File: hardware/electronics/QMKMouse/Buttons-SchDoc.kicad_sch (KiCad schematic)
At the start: 8 parts

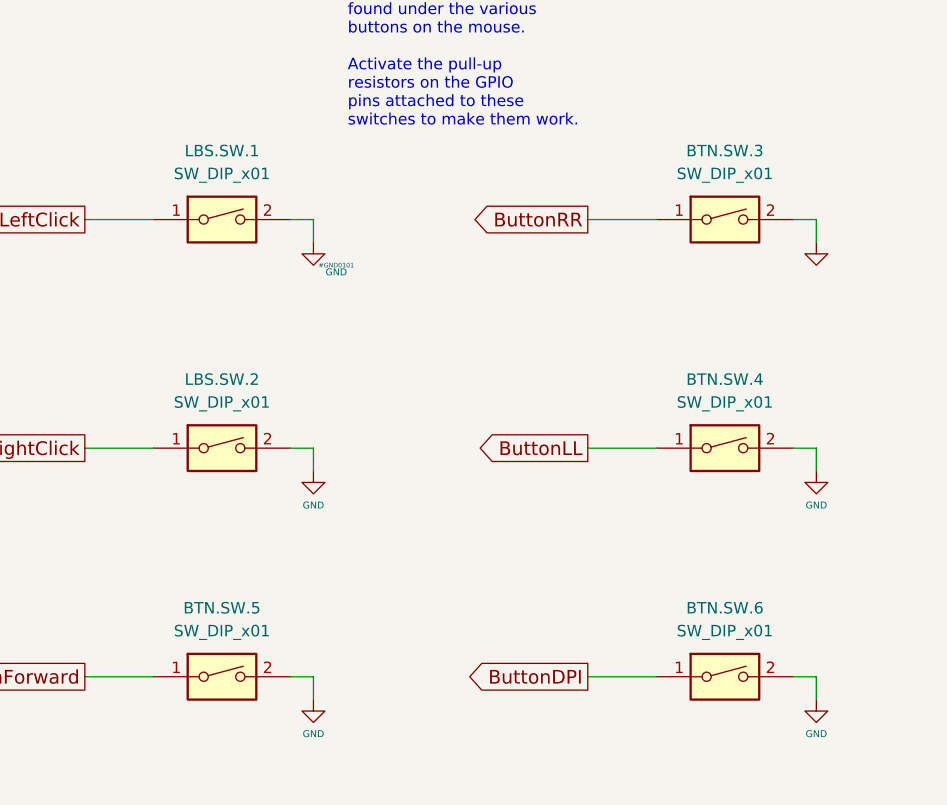
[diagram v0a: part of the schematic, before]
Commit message: update schematic components
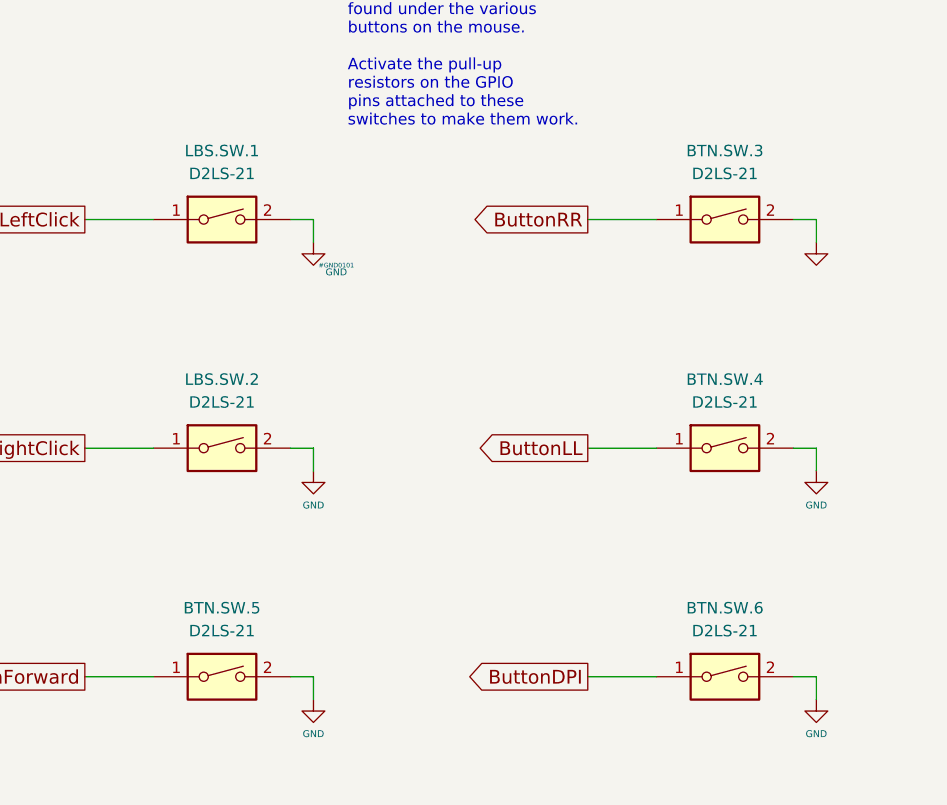
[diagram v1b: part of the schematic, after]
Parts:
- BTN.SW.3, BTN.SW.4, BTN.SW.5, BTN.SW.6, LBS.SW.1, LBS.SW.2: value SW_DIP_x01 -> D2LS-21
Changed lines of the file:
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@@
     (in_bom yes) (on_board yes) (fields_autoplaced)
     (property "Reference" "LBS.SW.2" (id 0) (at 91.44 87.63 0))
-    (property "Value" "SW_DIP_x01" (id 1) (at 91.44 90.17 0))
+    (property "Value" "D2LS-21" (id 1) (at 91.44 90.17 0))
     (property "Footprint" "" (id 2) (at 91.44 95.25 0)
       (effects (font (size 1.27 1.27)) hide)
@@
     (in_bom yes) (on_board yes) (fields_autoplaced)
     (property "Reference" "BTN.SW.4" (id 0) (at 147.32 87.63 0))
-    (property "Value" "SW_DIP_x01" (id 1) (at 147.32 90.17 0))
+    (property "Value" "D2LS-21" (id 1) (at 147.32 90.17 0))
     (property "Footprint" "" (id 2) (at 147.32 95.25 0)
       (effects (font (size 1.27 1.27)) hide)
@@
     (in_bom yes) (on_board yes) (fields_autoplaced)
     (property "Reference" "BTN.SW.6" (id 0) (at 147.32 113.03 0))
-    (property "Value" "SW_DIP_x01" (id 1) (at 147.32 115.57 0))
+    (property "Value" "D2LS-21" (id 1) (at 147.32 115.57 0))
     (property "Footprint" "" (id 2) (at 147.32 120.65 0)
       (effects (font (size 1.27 1.27)) hide)
@@
     (in_bom yes) (on_board yes) (fields_autoplaced)
     (property "Reference" "BTN.SW.5" (id 0) (at 91.44 113.03 0))
-    (property "Value" "SW_DIP_x01" (id 1) (at 91.44 115.57 0))
+    (property "Value" "D2LS-21" (id 1) (at 91.44 115.57 0))
     (property "Footprint" "" (id 2) (at 91.44 120.65 0)
       (effects (font (size 1.27 1.27)) hide)
@@
     (in_bom yes) (on_board yes) (fields_autoplaced)
     (property "Reference" "LBS.SW.1" (id 0) (at 91.44 62.23 0))
-    (property "Value" "SW_DIP_x01" (id 1) (at 91.44 64.77 0))
+    (property "Value" "D2LS-21" (id 1) (at 91.44 64.77 0))
     (property "Footprint" "" (id 2) (at 91.44 69.85 0)
       (effects (font (size 1.27 1.27)) hide)
@@
     (in_bom yes) (on_board yes) (fields_autoplaced)
     (property "Reference" "BTN.SW.3" (id 0) (at 147.32 62.23 0))
-    (property "Value" "SW_DIP_x01" (id 1) (at 147.32 64.77 0))
+    (property "Value" "D2LS-21" (id 1) (at 147.32 64.77 0))
     (property "Footprint" "" (id 2) (at 147.32 69.85 0)
       (effects (font (size 1.27 1.27)) hide)

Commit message: update schematic from PCB; sync netlist and fix some symbol orientations; also fix LED symbol
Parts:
- BTN.SW.3, BTN.SW.4, BTN.SW.5, BTN.SW.6, BTN.SW.7, BTN.SW.8, LBS.SW.1, LBS.SW.2: footprint (none) -> Switches.PcbLib:D2LS-21
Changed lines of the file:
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@@
     (property "Reference" "BTN.SW.7" (id 0) (at 91.44 138.43 0))
     (property "Value" "SW_DIP_x01" (id 1) (at 91.44 140.97 0))
-    (property "Footprint" "" (id 2) (at 91.44 146.05 0)
+    (property "Footprint" "Switches.PcbLib:D2LS-21" (id 2) (at 91.44 146.05 0)
       (effects (font (size 1.27 1.27)) hide)
     )
@@
     (property "Reference" "LBS.SW.2" (id 0) (at 91.44 87.63 0))
     (property "Value" "D2LS-21" (id 1) (at 91.44 90.17 0))
-    (property "Footprint" "" (id 2) (at 91.44 95.25 0)
+    (property "Footprint" "Switches.PcbLib:D2LS-21" (id 2) (at 91.44 95.25 0)
       (effects (font (size 1.27 1.27)) hide)
     )
@@
     (property "Reference" "BTN.SW.4" (id 0) (at 147.32 87.63 0))
     (property "Value" "D2LS-21" (id 1) (at 147.32 90.17 0))
-    (property "Footprint" "" (id 2) (at 147.32 95.25 0)
+    (property "Footprint" "Switches.PcbLib:D2LS-21" (id 2) (at 147.32 95.25 0)
       (effects (font (size 1.27 1.27)) hide)
     )
@@
     (property "Reference" "BTN.SW.6" (id 0) (at 147.32 113.03 0))
     (property "Value" "D2LS-21" (id 1) (at 147.32 115.57 0))
-    (property "Footprint" "" (id 2) (at 147.32 120.65 0)
+    (property "Footprint" "Switches.PcbLib:D2LS-21" (id 2) (at 147.32 120.65 0)
       (effects (font (size 1.27 1.27)) hide)
     )
@@
     (property "Reference" "BTN.SW.8" (id 0) (at 147.32 138.43 0))
     (property "Value" "SW_DIP_x01" (id 1) (at 147.32 140.97 0))
-    (property "Footprint" "" (id 2) (at 147.32 146.05 0)
+    (property "Footprint" "Switches.PcbLib:D2LS-21" (id 2) (at 147.32 146.05 0)
       (effects (font (size 1.27 1.27)) hide)
     )
@@
     (property "Reference" "BTN.SW.5" (id 0) (at 91.44 113.03 0))
     (property "Value" "D2LS-21" (id 1) (at 91.44 115.57 0))
-    (property "Footprint" "" (id 2) (at 91.44 120.65 0)
+    (property "Footprint" "Switches.PcbLib:D2LS-21" (id 2) (at 91.44 120.65 0)
       (effects (font (size 1.27 1.27)) hide)
     )
@@
     (property "Reference" "LBS.SW.1" (id 0) (at 91.44 62.23 0))
     (property "Value" "D2LS-21" (id 1) (at 91.44 64.77 0))
-    (property "Footprint" "" (id 2) (at 91.44 69.85 0)
+    (property "Footprint" "Switches.PcbLib:D2LS-21" (id 2) (at 91.44 69.85 0)
       (effects (font (size 1.27 1.27)) hide)
     )
@@
     (property "Reference" "BTN.SW.3" (id 0) (at 147.32 62.23 0))
     (property "Value" "D2LS-21" (id 1) (at 147.32 64.77 0))
-    (property "Footprint" "" (id 2) (at 147.32 69.85 0)
+    (property "Footprint" "Switches.PcbLib:D2LS-21" (id 2) (at 147.32 69.85 0)
       (effects (font (size 1.27 1.27)) hide)
     )

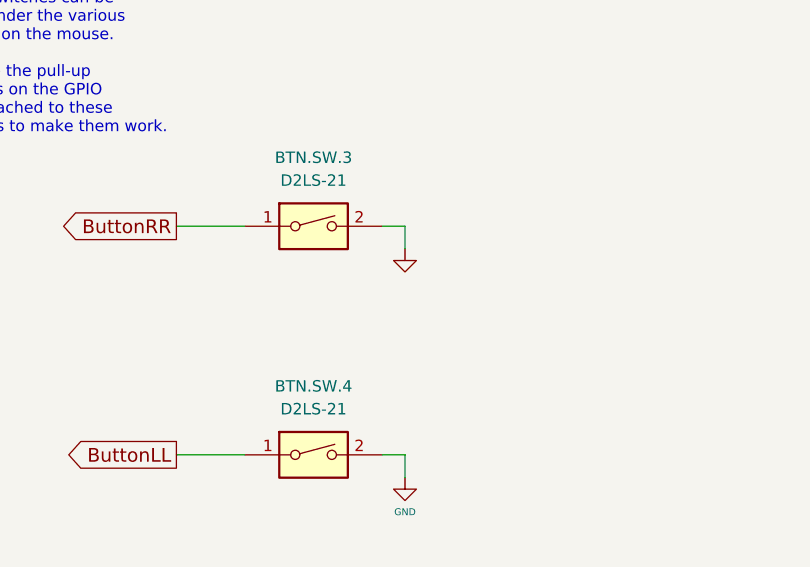
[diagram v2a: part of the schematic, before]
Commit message: Fix some schematic PCB mismatch
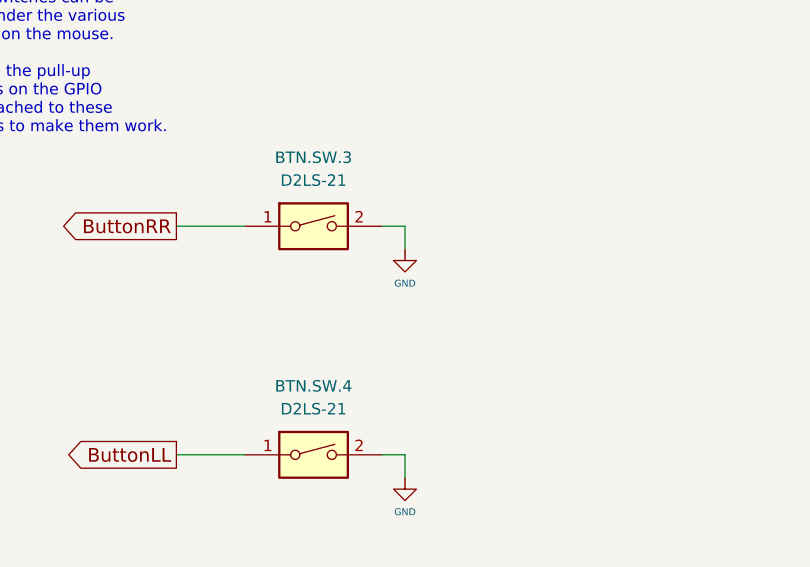
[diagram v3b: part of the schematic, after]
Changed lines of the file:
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@@
       (effects (font (size 0.508 0.508)) hide)
     )
-    (property "Value" "GND" (id 1) (at 160.02 75.692 0)
-      (effects (font (size 0.762 0.762)) hide)
+    (property "Value" "GND" (id 1) (at 157.48 76.2 0)
+      (effects (font (size 0.762 0.762)))
     )
     (property "Footprint" "" (id 2) (at 157.48 72.39 0)

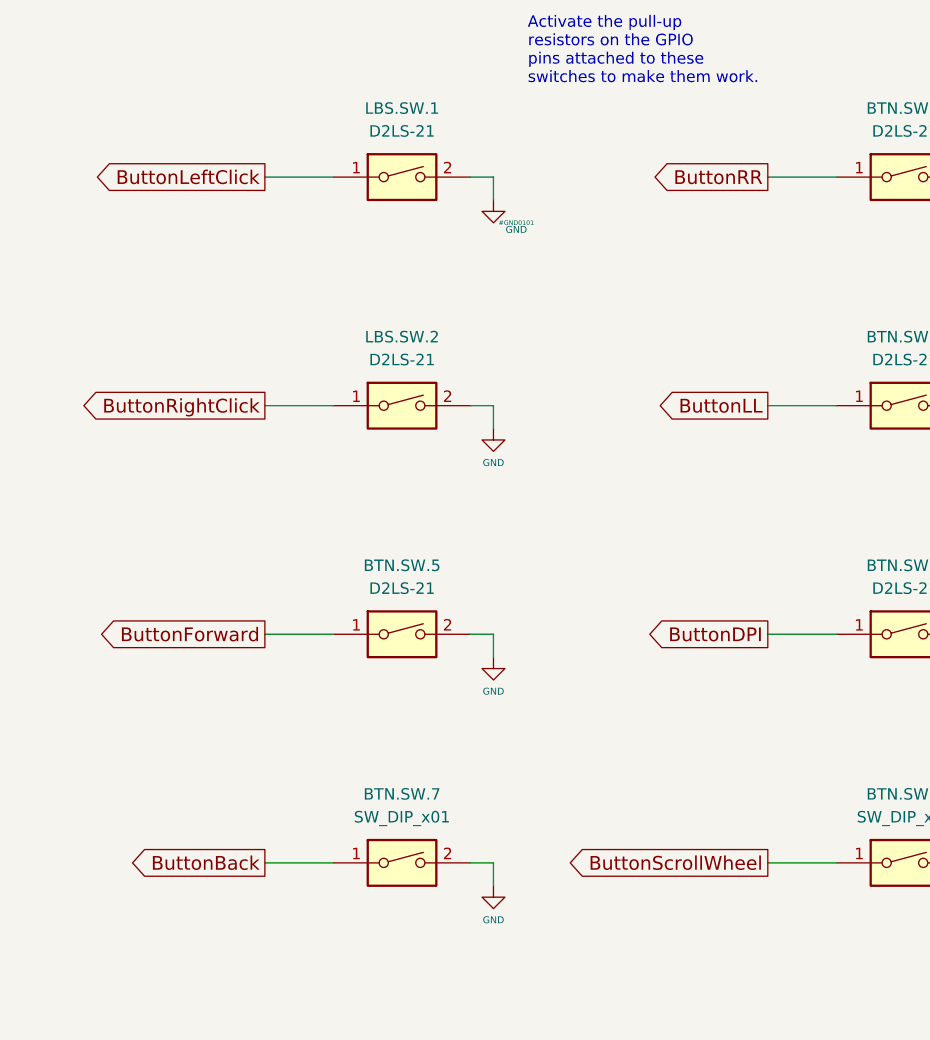
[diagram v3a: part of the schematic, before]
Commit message: fix ERC errors and use hierarchy labels
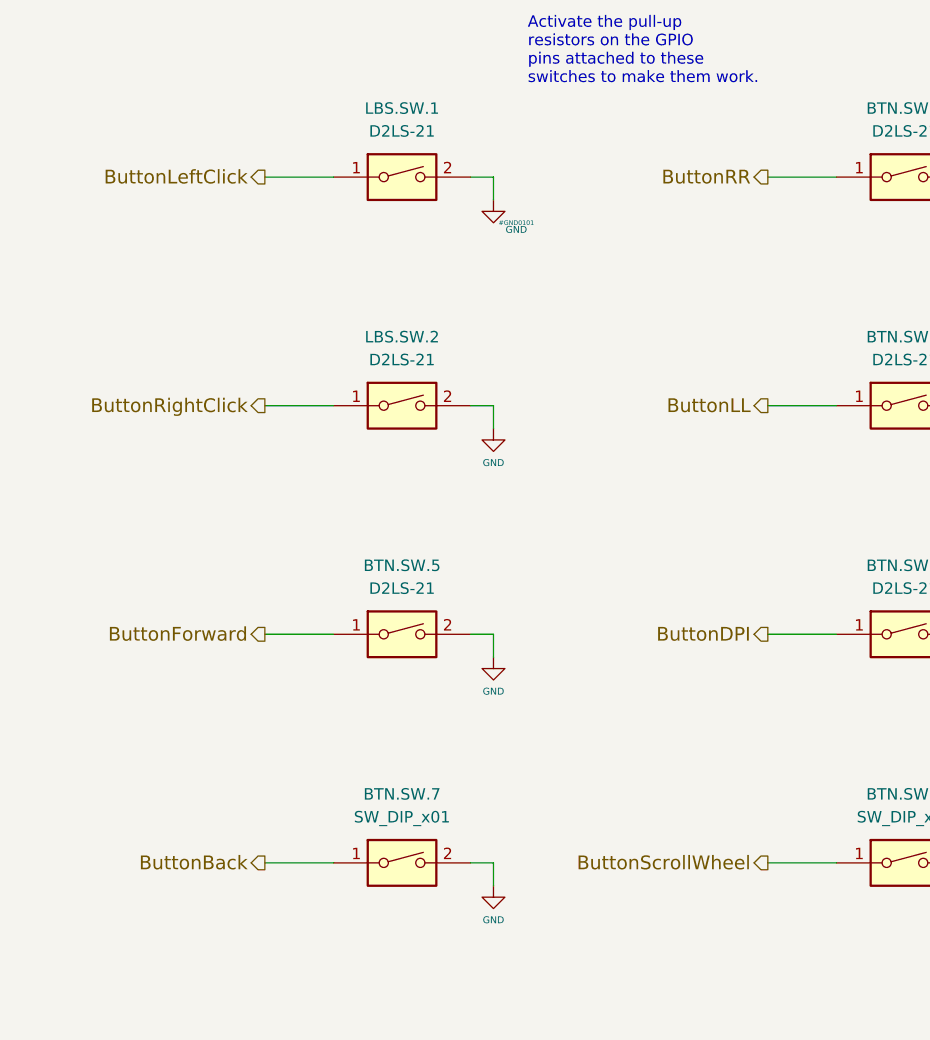
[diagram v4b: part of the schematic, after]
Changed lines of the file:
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@@
     (effects (font (size 1.3716 1.3716)) (justify left bottom))
   )
-  (global_label "ButtonLL" (shape output) (at 132.08 95.25 180) (fields_autoplaced)
+  (hierarchical_label "ButtonRightClick" (shape output) (at 76.2 95.25 180)
     (effects (font (size 1.524 1.524)) (justify right))
-    (property "Intersheet References" "${INTERSHEET_REFS}" (id 0) (at 284.48 -57.15 0)
-      (effects (font (size 1.27 1.27)) (justify left) hide)
-    )
   )
-  (global_label "ButtonDPI" (shape output) (at 132.08 120.65 180) (fields_autoplaced)
+  (hierarchical_label "ButtonDPI" (shape output) (at 132.08 120.65 180)
     (effects (font (size 1.524 1.524)) (justify right))
-    (property "Intersheet References" "${INTERSHEET_REFS}" (id 0) (at 284.48 -57.15 0)
-      (effects (font (size 1.27 1.27)) (justify left) hide)
-    )
   )
-  (global_label "ButtonBack" (shape output) (at 76.2 146.05 180) (fields_autoplaced)
+  (hierarchical_label "ButtonScrollWheel" (shape output) (at 132.08 146.05 180)
     (effects (font (size 1.524 1.524)) (justify right))
-    (property "Intersheet References" "${INTERSHEET_REFS}" (id 0) (at 152.4 -57.15 0)
-      (effects (font (size 1.27 1.27)) (justify left) hide)
-    )
   )
-  (global_label "ButtonRightClick" (shape output) (at 76.2 95.25 180) (fields_autoplaced)
+  (hierarchical_label "ButtonLL" (shape output) (at 132.08 95.25 180)
     (effects (font (size 1.524 1.524)) (justify right))
-    (property "Intersheet References" "${INTERSHEET_REFS}" (id 0) (at 152.4 -57.15 0)
-      (effects (font (size 1.27 1.27)) (justify left) hide)
-    )
   )
-  (global_label "ButtonForward" (shape output) (at 76.2 120.65 180) (fields_autoplaced)
+  (hierarchical_label "ButtonBack" (shape output) (at 76.2 146.05 180)
     (effects (font (size 1.524 1.524)) (justify right))
-    (property "Intersheet References" "${INTERSHEET_REFS}" (id 0) (at 152.4 -57.15 0)
-      (effects (font (size 1.27 1.27)) (justify left) hide)
-    )
   )
-  (global_label "ButtonScrollWheel" (shape output) (at 132.08 146.05 180) (fields_autoplaced)
+  (hierarchical_label "ButtonRR" (shape output) (at 132.08 69.85 180)
     (effects (font (size 1.524 1.524)) (justify right))
-    (property "Intersheet References" "${INTERSHEET_REFS}" (id 0) (at 284.48 -57.15 0)
-      (effects (font (size 1.27 1.27)) (justify left) hide)
-    )
   )
-  (global_label "ButtonLeftClick" (shape output) (at 76.2 69.85 180) (fields_autoplaced)
+  (hierarchical_label "ButtonLeftClick" (shape output) (at 76.2 69.85 180)
     (effects (font (size 1.524 1.524)) (justify right))
-    (property "Intersheet References" "${INTERSHEET_REFS}" (id 0) (at 152.4 -57.15 0)
-      (effects (font (size 1.27 1.27)) (justify left) hide)
-    )
   )
-  (global_label "ButtonRR" (shape output) (at 132.08 69.85 180) (fields_autoplaced)
+  (hierarchical_label "ButtonForward" (shape output) (at 76.2 120.65 180)
     (effects (font (size 1.524 1.524)) (justify right))
-    (property "Intersheet References" "${INTERSHEET_REFS}" (id 0) (at 284.48 -57.15 0)
-      (effects (font (size 1.27 1.27)) (justify left) hide)
-    )
   )
   (symbol (lib_id "power:GND") (at 101.6 148.59 0) (unit 1)

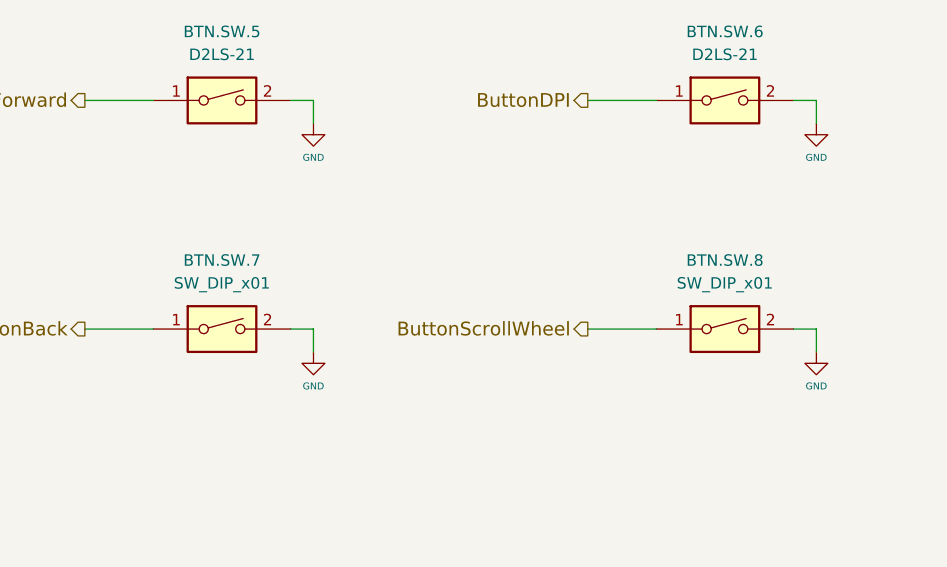
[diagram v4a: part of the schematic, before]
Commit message: fix minor Schematic naming errors; improve BoM generation
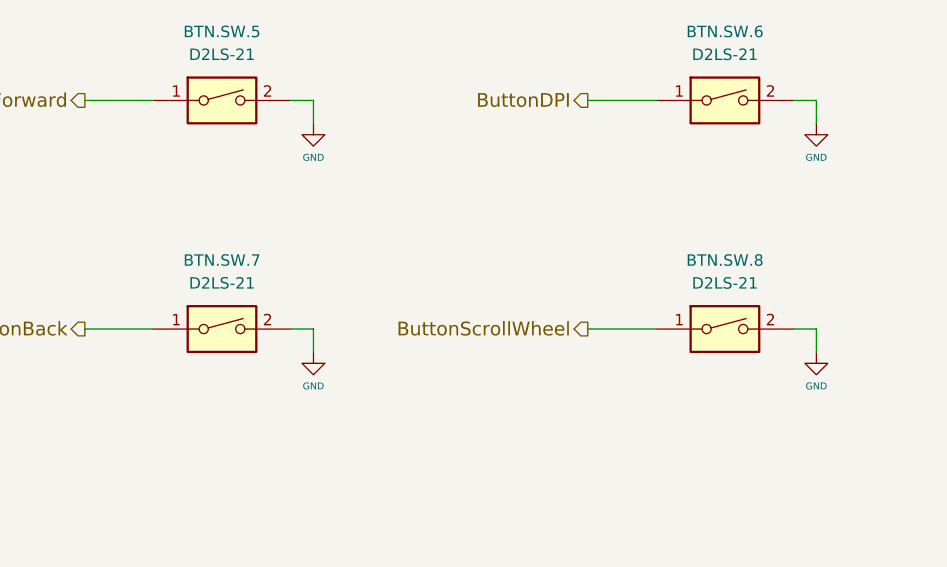
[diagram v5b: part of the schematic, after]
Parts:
- BTN.SW.7, BTN.SW.8: value SW_DIP_x01 -> D2LS-21
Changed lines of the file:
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@@
     (in_bom yes) (on_board yes) (fields_autoplaced)
     (property "Reference" "BTN.SW.7" (id 0) (at 91.44 138.43 0))
-    (property "Value" "SW_DIP_x01" (id 1) (at 91.44 140.97 0))
+    (property "Value" "D2LS-21" (id 1) (at 91.44 140.97 0))
     (property "Footprint" "Switches.PcbLib:D2LS-21" (id 2) (at 91.44 146.05 0)
       (effects (font (size 1.27 1.27)) hide)
@@
     (in_bom yes) (on_board yes) (fields_autoplaced)
     (property "Reference" "BTN.SW.8" (id 0) (at 147.32 138.43 0))
-    (property "Value" "SW_DIP_x01" (id 1) (at 147.32 140.97 0))
+    (property "Value" "D2LS-21" (id 1) (at 147.32 140.97 0))
     (property "Footprint" "Switches.PcbLib:D2LS-21" (id 2) (at 147.32 146.05 0)
       (effects (font (size 1.27 1.27)) hide)
